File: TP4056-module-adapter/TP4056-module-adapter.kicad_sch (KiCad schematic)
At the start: 12 parts, among them J1 Conn_01x01, J2 Conn_01x01, J3 Conn_01x01, J4 Conn_01x01, J5 Conn_01x01, J6 Conn_01x01, Q1 SI2301, Q2 SI2301

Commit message: board layout
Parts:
- removed J5, J6: Conn_01x01, Connector_PinHeader_2.54mm:PinHeader_1x01_P2.54mm_Vertical, symbol Connector_Generic:Conn_01x01
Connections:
- net -BATT is gone; now on net VCC: J4.1 (Pin_1)
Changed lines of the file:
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@@
-    (stroke (width 0) (type default))
-  )
-  (wire (pts (xy 199.39 67.31) (xy 199.39 68.58))
     (stroke (width 0) (type default))
   )
@@
     (stroke (width 0) (type default))
   )
-  (wire (pts (xy 213.36 67.31) (xy 213.36 68.58))
-    (stroke (width 0) (type default))
-  )
   (wire (pts (xy 135.89 53.34) (xy 138.43 53.34))
     (stroke (width 0) (type default))
@@
     (stroke (width 0) (type default))
   )
-  (wire (pts (xy 212.09 67.31) (xy 213.36 67.31))
-    (stroke (width 0) (type default))
-  )
   (wire (pts (xy 106.68 64.77) (xy 113.03 64.77))
     (stroke (width 0) (type default))
@@
   )
   (wire (pts (xy 118.11 74.93) (xy 138.43 74.93))
-    (stroke (width 0) (type default))
-  )
-  (wire (pts (xy 198.12 67.31) (xy 199.39 67.31))
     (stroke (width 0) (type default))
   )
@@
     )
   )
-  (symbol (lib_id "power:GND") (at 213.36 68.58 0) (unit 1)
-    (in_bom yes) (on_board yes) (dnp no) (fields_autoplaced)
-    (property "Reference" "#PWR010" (at 213.36 74.93 0)
-      (effects (font (size 1.27 1.27)) hide)
-    )
-    (property "Value" "GND" (at 213.36 73.66 0)
-      (effects (font (size 1.27 1.27)))
-    )
-    (property "Footprint" "" (at 213.36 68.58 0)
-      (effects (font (size 1.27 1.27)) hide)
-    )
-    (property "Datasheet" "" (at 213.36 68.58 0)
-      (effects (font (size 1.27 1.27)) hide)
-    )
-    (pin "1")
-    (instances
-      (project "TP4056-module-adapter"
-        (path "/bf0c3ad5-dd7c-4c9b-a4b0-8fb0fafb42b3"
-          (reference "#PWR010") (unit 1)
-        )
-      )
-    )
-  )
   (symbol (lib_id "power:VBUS") (at 106.68 52.07 0) (unit 1)
     (in_bom yes) (on_board yes) (dnp no) (fields_autoplaced)
@@
     )
   )
+  (symbol (lib_id "Connector_Generic:Conn_01x01") (at 207.01 62.23 0) (mirror y) (unit 1)
+    (in_bom yes) (on_board yes) (dnp no)
+    (property "Reference" "J4" (at 204.47 62.23 0)
+      (effects (font (size 1.27 1.27)) (justify left))
+    )
+    (property "Value" "Conn_01x01" (at 204.47 63.5 0)
+      (effects (font (size 1.27 1.27)) (justify left) hide)
+    )
+    (property "Footprint" "Connector_PinHeader_2.54mm:PinHeader_1x01_P2.54mm_Vertical" (at 207.01 62.23 0)
+      (effects (font (size 1.27 1.27)) hide)
+    )
+    (property "Datasheet" "~" (at 207.01 62.23 0)
+      (effects (font (size 1.27 1.27)) hide)
+    )
+    (pin "1")
+    (instances
+      (project "TP4056-module-adapter"
+        (path "/bf0c3ad5-dd7c-4c9b-a4b0-8fb0fafb42b3"
+          (reference "J4") (unit 1)
+        )
+      )
+      (project "LiPo_BuckBoost_Charger"
+        (path "/ebf16ca0-689c-447d-aaab-3c694dddd46d"
+          (reference "J3") (unit 1)
+        )
+      )
+    )
+  )
   (symbol (lib_id "power:VCC") (at 138.43 52.07 0) (unit 1)
     (in_bom yes) (on_board yes) (dnp no)
@@
     )
   )
-  (symbol (lib_id "Connector_Generic:Conn_01x01") (at 207.01 67.31 0) (mirror y) (unit 1)
-    (in_bom yes) (on_board yes) (dnp no)
-    (property "Reference" "J6" (at 204.47 67.31 0)
-      (effects (font (size 1.27 1.27)) (justify left))
-    )
-    (property "Value" "Conn_01x01" (at 204.47 68.58 0)
-      (effects (font (size 1.27 1.27)) (justify left) hide)
-    )
-    (property "Footprint" "Connector_PinHeader_2.54mm:PinHeader_1x01_P2.54mm_Vertical" (at 207.01 67.31 0)
-      (effects (font (size 1.27 1.27)) hide)
-    )
-    (property "Datasheet" "~" (at 207.01 67.31 0)
-      (effects (font (size 1.27 1.27)) hide)
-    )
-    (pin "1")
-    (instances
-      (project "TP4056-module-adapter"
-        (path "/bf0c3ad5-dd7c-4c9b-a4b0-8fb0fafb42b3"
-          (reference "J6") (unit 1)
-        )
-      )
-      (project "LiPo_BuckBoost_Charger"
-        (path "/ebf16ca0-689c-447d-aaab-3c694dddd46d"
-          (reference "J4") (unit 1)
-        )
-      )
-    )
-  )
   (symbol (lib_id "Device:R") (at 121.92 58.42 0) (unit 1)
     (in_bom yes) (on_board yes) (dnp no)
@@
     )
   )
-  (symbol (lib_id "Connector_Generic:Conn_01x01") (at 193.04 67.31 0) (mirror y) (unit 1)
-    (in_bom yes) (on_board yes) (dnp no)
-    (property "Reference" "J4" (at 190.5 67.31 0)
-      (effects (font (size 1.27 1.27)) (justify left))
-    )
-    (property "Value" "Conn_01x01" (at 190.5 68.58 0)
-      (effects (font (size 1.27 1.27)) (justify left) hide)
-    )
-    (property "Footprint" "Connector_PinHeader_2.54mm:PinHeader_1x01_P2.54mm_Vertical" (at 193.04 67.31 0)
-      (effects (font (size 1.27 1.27)) hide)
-    )
-    (property "Datasheet" "~" (at 193.04 67.31 0)
-      (effects (font (size 1.27 1.27)) hide)
-    )
-    (pin "1")
-    (instances
-      (project "TP4056-module-adapter"
-        (path "/bf0c3ad5-dd7c-4c9b-a4b0-8fb0fafb42b3"
-          (reference "J4") (unit 1)
-        )
-      )
-      (project "LiPo_BuckBoost_Charger"
-        (path "/ebf16ca0-689c-447d-aaab-3c694dddd46d"
-          (reference "J4") (unit 1)
-        )
-      )
-    )
-  )
   (symbol (lib_id "Device:D_Schottky") (at 132.08 53.34 0) (mirror y) (unit 1)
     (in_bom yes) (on_board yes) (dnp no)
@@
         (path "/ebf16ca0-689c-447d-aaab-3c694dddd46d"
           (reference "D4") (unit 1)
-        )
-      )
-    )
-  )
-  (symbol (lib_id "power:-BATT") (at 199.39 68.58 180) (unit 1)
-    (in_bom yes) (on_board yes) (dnp no) (fields_autoplaced)
-    (property "Reference" "#PWR08" (at 199.39 64.77 0)
-      (effects (font (size 1.27 1.27)) hide)
-    )
-    (property "Value" "-BATT" (at 199.39 73.66 0)
-      (effects (font (size 1.27 1.27)))
-    )
-    (property "Footprint" "" (at 199.39 68.58 0)
-      (effects (font (size 1.27 1.27)) hide)
-    )
-    (property "Datasheet" "" (at 199.39 68.58 0)
-      (effects (font (size 1.27 1.27)) hide)
-    )
-    (pin "1")
-    (instances
-      (project "TP4056-module-adapter"
-        (path "/bf0c3ad5-dd7c-4c9b-a4b0-8fb0fafb42b3"
-          (reference "#PWR08") (unit 1)
-        )
-      )
-      (project "LiPo_BuckBoost_Charger"
-        (path "/ebf16ca0-689c-447d-aaab-3c694dddd46d"
-          (reference "#PWR032") (unit 1)
         )
       )
@@
         )
       )
-    )
-  )
-  (symbol (lib_id "Connector_Generic:Conn_01x01") (at 207.01 62.23 0) (mirror y) (unit 1)
-    (in_bom yes) (on_board yes) (dnp no)
-    (property "Reference" "J5" (at 204.47 62.23 0)
-      (effects (font (size 1.27 1.27)) (justify left))
-    )
-    (property "Value" "Conn_01x01" (at 204.47 63.5 0)
-      (effects (font (size 1.27 1.27)) (justify left) hide)
-    )
-    (property "Footprint" "Connector_PinHeader_2.54mm:PinHeader_1x01_P2.54mm_Vertical" (at 207.01 62.23 0)
-      (effects (font (size 1.27 1.27)) hide)
-    )
-    (property "Datasheet" "~" (at 207.01 62.23 0)
-      (effects (font (size 1.27 1.27)) hide)
-    )
-    (pin "1")
-    (instances
-      (project "TP4056-module-adapter"
-        (path "/bf0c3ad5-dd7c-4c9b-a4b0-8fb0fafb42b3"
-          (reference "J5") (unit 1)
-        )
-      )
-      (project "LiPo_BuckBoost_Charger"
-        (path "/ebf16ca0-689c-447d-aaab-3c694dddd46d"
-          (reference "J3") (unit 1)
-        )
-      )

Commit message: layout update
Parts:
- added J5: Conn_01x01, Connector_PinHeader_2.54mm:PinHeader_1x01_P2.54mm_Vertical, symbol Connector_Generic:Conn_01x01
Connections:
- net +BATT: now also J5.1 (Pin_1); no longer J3.1 (Pin_1)
- net LINE: now reaches F1.2, Q1.2 (S)
- net LINE: now also J3.1 (Pin_1)
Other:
- moved on the sheet: J1, J2

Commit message: v1.2 - ready for ordering
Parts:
- removed J1, J2, J3, J4, J5: Conn_01x01, Connector_PinHeader_2.54mm:PinHeader_1x01_P2.54mm_Vertical, symbol Connector_Generic:Conn_01x01
- added H1: MountingHole, MountingHole:MountingHole_2.2mm_M2_DIN965_Pad, symbol Mechanical:MountingHole
- added J1, J2: Conn_01x02, Connector_PinHeader_2.54mm:PinHeader_1x02_P2.54mm_Vertical, symbol Connector_Generic:Conn_01x02
- added J3: Conn_01x03, Connector_PinHeader_2.54mm:PinHeader_1x03_P2.54mm_Vertical, symbol Connector_Generic:Conn_01x03
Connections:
- net +BATT: now also J2.1 (Pin_1)
- net GND: now also J1.1 (Pin_1), J3.1 (Pin_1)
- net LINE: now also J2.2 (Pin_2)
- net VBUS: now also J1.2 (Pin_2)
- net VCC: now also J3.2 (Pin_2), J3.3 (Pin_3)

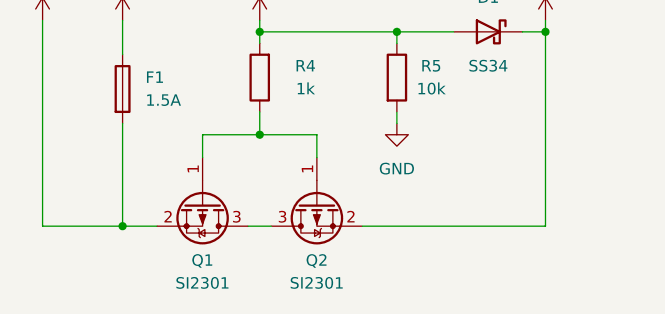
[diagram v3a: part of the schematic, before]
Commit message: updated wrong pmos in schematic
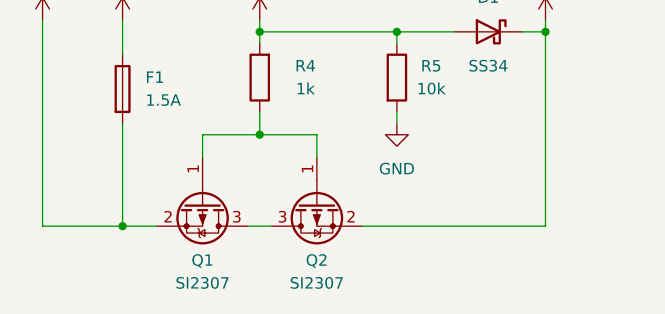
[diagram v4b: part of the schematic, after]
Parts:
- Q1, Q2: value SI2301 -> SI2307
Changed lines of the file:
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@@
       (effects (font (size 1.27 1.27)))
     )
-    (property "Value" "SI2301" (at 100.33 81.28 90)
+    (property "Value" "SI2307" (at 100.33 81.28 90)
       (effects (font (size 1.27 1.27)))
     )
@@
       (effects (font (size 1.27 1.27)))
     )
-    (property "Value" "SI2301" (at 113.03 81.28 90)
+    (property "Value" "SI2307" (at 113.03 81.28 90)
       (effects (font (size 1.27 1.27)))
     )
